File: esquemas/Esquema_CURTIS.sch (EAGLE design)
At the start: 18 parts

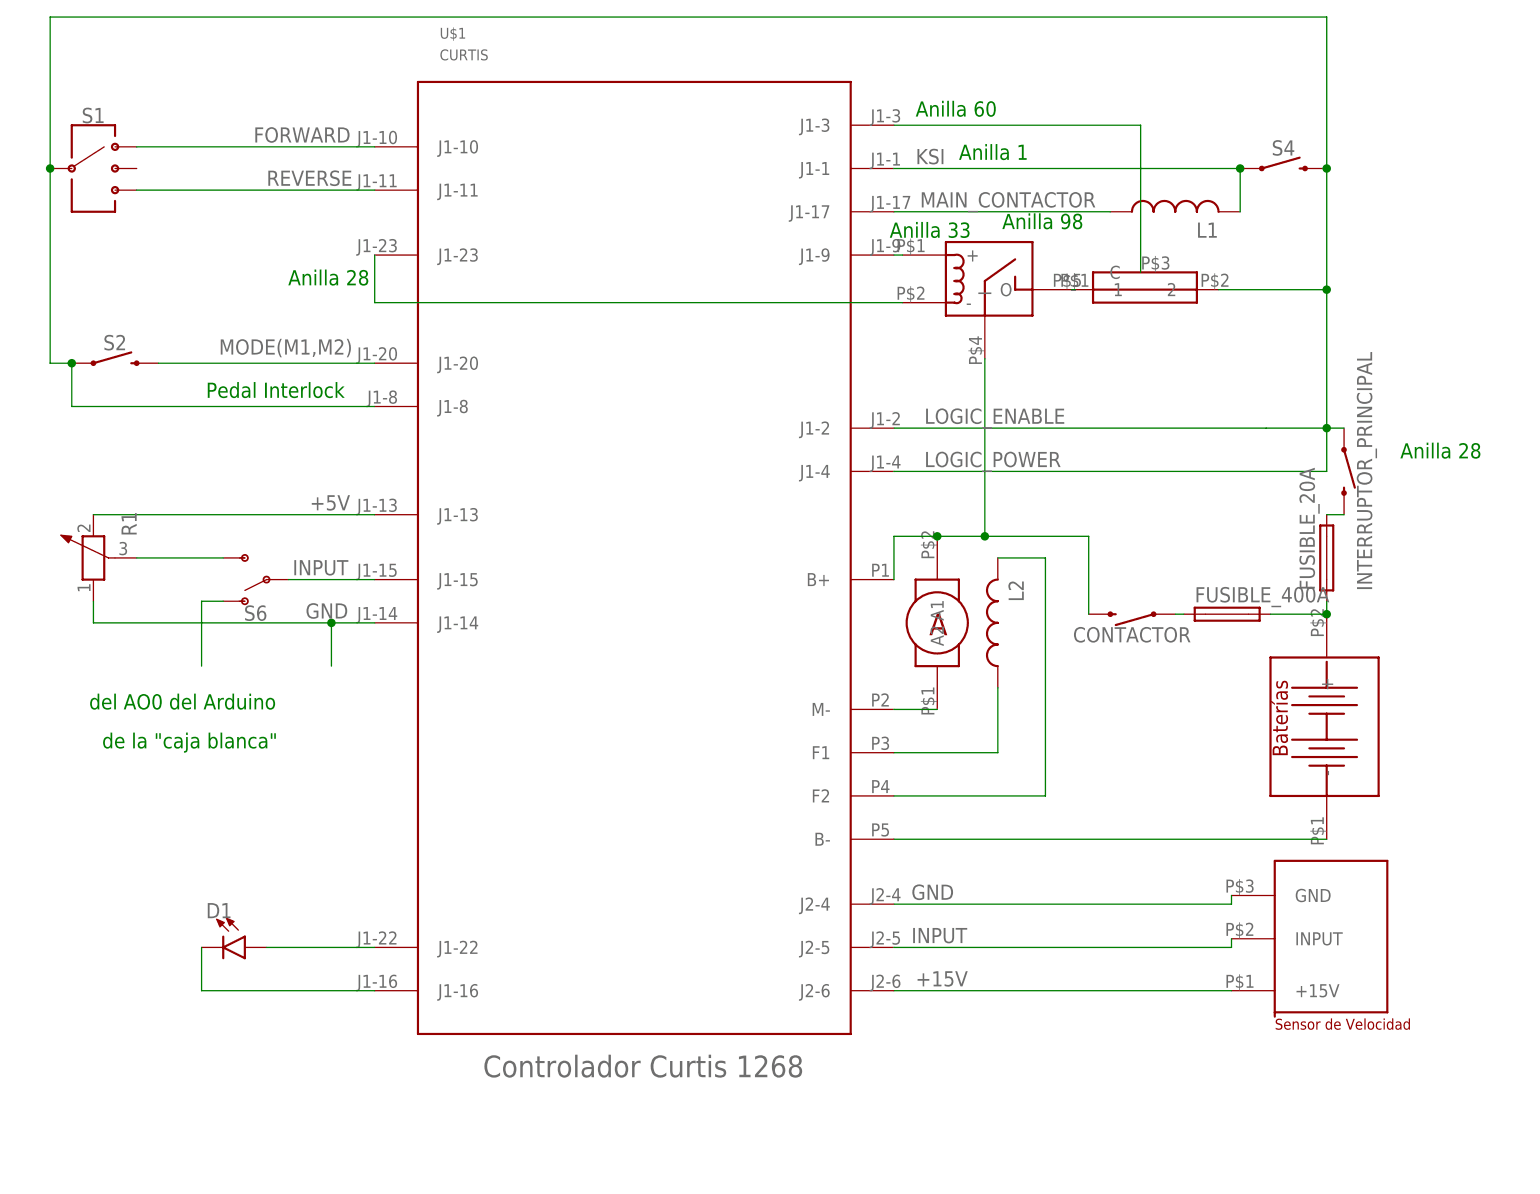
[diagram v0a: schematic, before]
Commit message: Modificación
Modificación del texto en PowerBox1, adición del programador en Curtis y
redistribución de algunos elementos
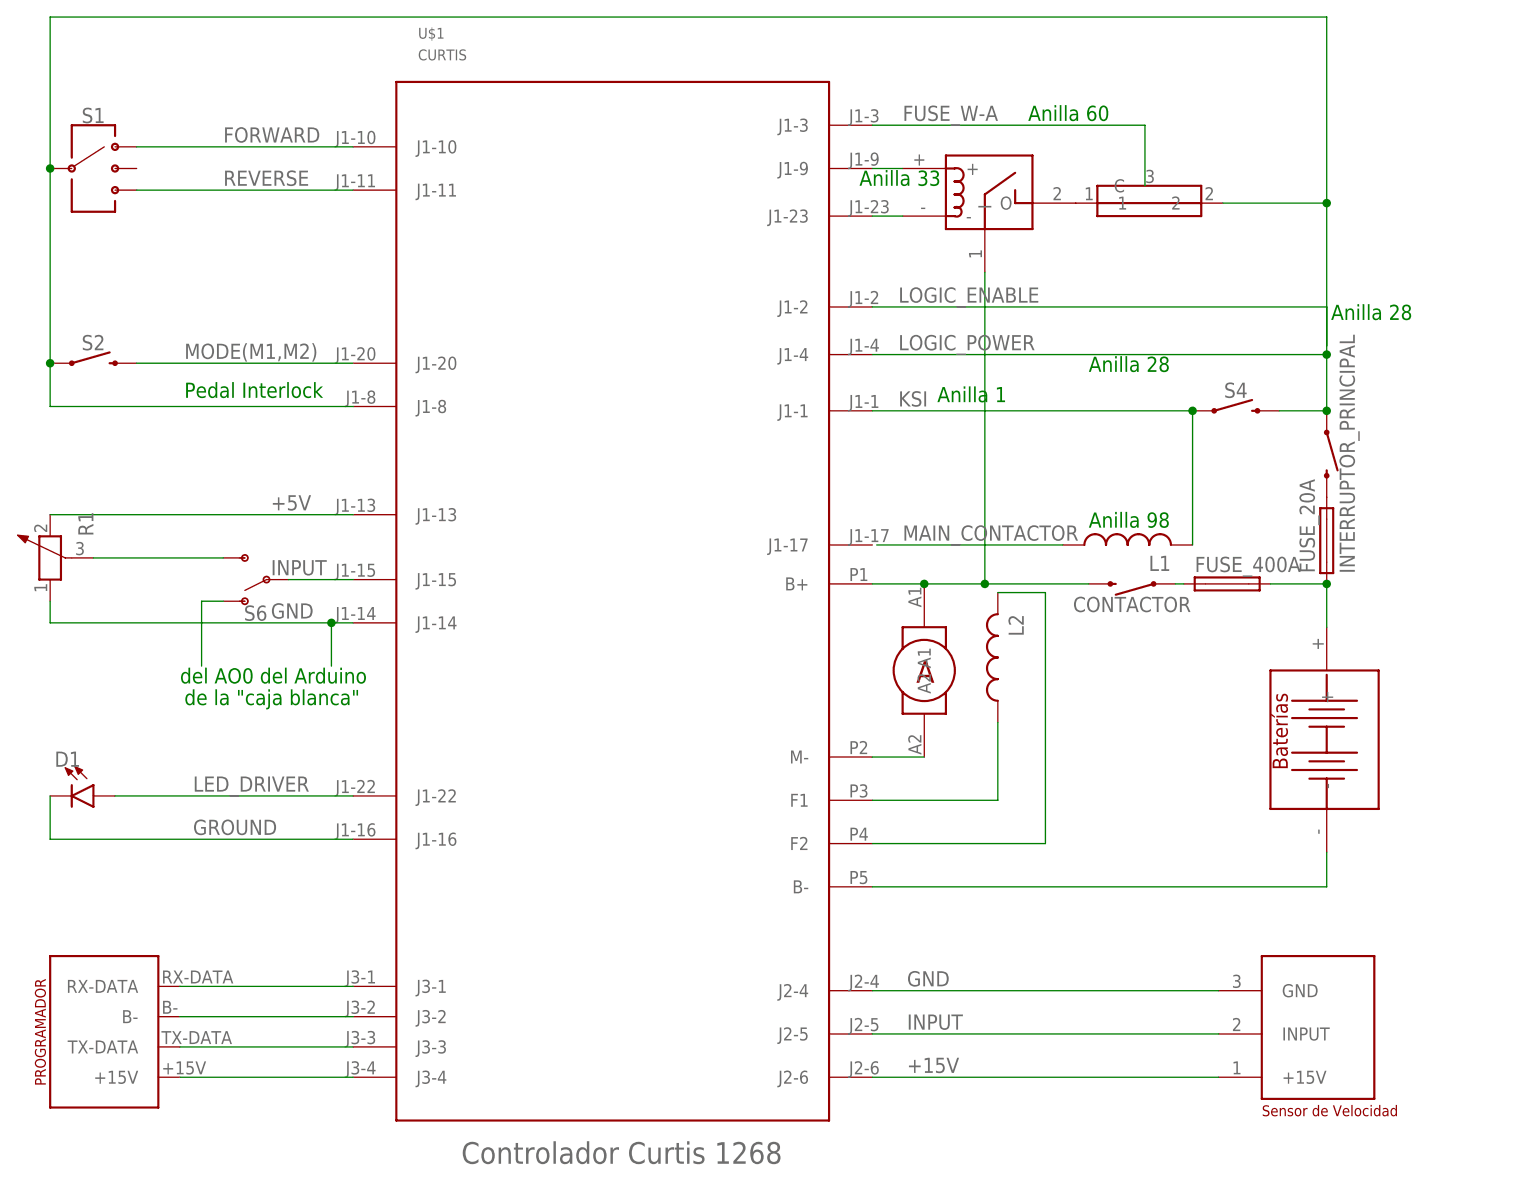
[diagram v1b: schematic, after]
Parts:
- removed FUSIBLE_20A, FUSIBLE_400A: (no value), fuse:GSH15
- added FUSE_20A, FUSE_400A: (no value), fuse:GSH15
- added U$3: PROGRAMADOR, ecar:PROGRAMADOR
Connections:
- net N$10 renamed GROUND
- net N$14 renamed FUSE_W-A
- net N$9 renamed LED_DRIVER
- removed net N$2 (its old number): U$1.M-, U$2.A2
- new net LOGIC_ENABLE: U$1.J1-2
- new net N$10: U$1.J3-2, U$3.B-
- new net N$12: U$1.J3-3, U$3.TX-DATA
- new net N$15: U$1.J3-4, U$3.+15V
- new net N$17: U$2.A2
- new net N$9: U$1.J3-1, U$3.RX-DATA
- net +15V: no longer U$1.J2-6
- net GND: no longer U$1.J2-4
- net INPUT: no longer U$1.J2-5
- net LOGIC_POWER: now also U$1.J1-4
- net MAIN_CONTACTOR: no longer U$1.J1-17
- net N$16: now also FUSE_20A.1, FUSE_400A.2; no longer FUSIBLE_20A.1, FUSIBLE_400A.2
- net N$3: now also FUSE_400A.1; no longer FUSIBLE_400A.1
- net N$4: no longer U$1.F1
- net N$5: now also FUSE_20A.2; no longer FUSIBLE_20A.2
- net N$8: no longer U$1.F2
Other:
- moved on the sheet: CONTACTOR, D1, INTERRUPTOR_PRINCIPAL, L1, L2, R1, S2, S4

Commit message: Conexión J1-1 a 48V
Modificación del interruptor denominado "Llave" de J1-1. Se suprime por
un cable a 48V
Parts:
- removed S4: (no value), SparkFun-Switches:MOMENTARY-SWITCH-SPST-PTH-6.0MM
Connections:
- removed net LOGIC_POWER: INTERRUPTOR_PRINCIPAL.1, S1.3, S2.1, S4.2, U$1.J1-4, U$1.J1-8, U$7.2
- net KSI: now also INTERRUPTOR_PRINCIPAL.1, S1.3, S2.1, U$1.J1-4, U$1.J1-8, U$7.2; no longer S4.1
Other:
- note added: "Anilla 4"
- note added: "Anilla 6"
- note added: "Anilla 67"
- note added: "Anilla 7"
- note added: "Anilla 90"
- note added: "Anilla 91"
- note added: "LOGIC_POWER"
- note added: "N"
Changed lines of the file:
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@@
 <setting verticaltext="up"/>
 </settings>
-<grid distance="0.02" unitdist="inch" unit="inch" style="lines" multiple="1" display="yes" altdistance="0.002" altunitdist="inch" altunit="inch"/>
+<grid distance="0.01" unitdist="inch" unit="inch" style="lines" multiple="1" display="yes" altdistance="0.001" altunitdist="inch" altunit="inch"/>
 <layers>
 <layer number="1" name="Top" color="4" fill="1" visible="no" active="no"/>
@@
 <part name="S1" library="SparkFun-Switches" deviceset="SWITCH-SP3T" device="-SMD"/>
 <part name="S2" library="SparkFun-Switches" deviceset="MOMENTARY-SWITCH-SPST" device="-PTH-6.0MM" value=" "/>
-<part name="S4" library="SparkFun-Switches" deviceset="MOMENTARY-SWITCH-SPST" device="-PTH-6.0MM" value=" "/>
 <part name="FUSE_20A" library="fuse" deviceset="GSH15" device=""/>
 <part name="R1" library="rcl" deviceset="POTENTIOMETER_" device="PT-10S"/>
@@
 <sheet>
 <plain>
-<text x="109.728" y="91.948" size="1.778" layer="91">Anilla 60</text>
+<text x="94.742" y="89.408" size="1.778" layer="91">Anilla 60</text>
 <text x="89.916" y="84.328" size="1.778" layer="91">Anilla 33</text>
 <text x="145.288" y="68.58" size="1.778" layer="91">Anilla 28</text>
 <text x="10.16" y="25.908" size="1.778" layer="91">del AO0 del Arduino</text>
 <text x="10.668" y="23.368" size="1.778" layer="91">de la "caja blanca"</text>
-<text x="116.84" y="62.484" size="1.778" layer="91">Anilla 28</text>
-<text x="99.06" y="58.928" size="1.778" layer="91">Anilla 1</text>
-<text x="116.84" y="44.196" size="1.778" layer="91">Anilla 98</text>
+<text x="112.014" y="67.818" size="1.778" layer="91">Anilla 28</text>
+<text x="112.268" y="55.372" size="1.778" layer="91">Anilla 1</text>
+<text x="108.204" y="39.878" size="1.778" layer="91">Anilla 98</text>
 <text x="10.668" y="59.436" size="1.778" layer="91">Pedal Interlock</text>
+<text x="88.9" y="77.724" size="1.778" layer="91">Anilla 28</text>
+<text x="22.86" y="43.18" size="1.778" layer="91">Anilla 6</text>
+<text x="25.654" y="30.48" size="1.778" layer="91">Anilla 7</text>
+<text x="24.13" y="36.068" size="1.778" layer="91">Anilla 4</text>
+<text x="5.588" y="86.106" size="1.778" layer="91">N</text>
+<text x="23.368" y="86.614" size="1.778" layer="91">Anilla 90</text>
+<text x="23.622" y="81.026" size="1.778" layer="91">Anilla 91</text>
+<text x="112.014" y="62.23" size="1.778" layer="91">Anilla 67</text>
+<text x="94.742" y="65.024" size="1.778" layer="91">LOGIC_POWER</text>
 </plain>
 <instances>
 <instance part="S1" gate="G$1" x="0" y="86.36"/>
 <instance part="S2" gate="G$1" x="0" y="63.5"/>
-<instance part="S4" gate="G$1" x="134.112" y="57.912"/>
 <instance part="FUSE_20A" gate="1" x="144.78" y="42.672" rot="R90"/>
 <instance part="R1" gate="1" x="-5.08" y="40.64" rot="R90"/>
@@
 </segment>
 </net>
-<net name="KSI" class="0">
-<segment>
-<pinref part="S4" gate="G$1" pin="1"/>
-<wire x1="129.032" y1="57.912" x2="91.44" y2="57.912" width="0.1524" layer="91"/>
-<pinref part="L1" gate="G$1" pin="2"/>
-<wire x1="129.032" y1="42.164" x2="129.032" y2="57.912" width="0.1524" layer="91"/>
-<junction x="129.032" y="57.912"/>
-<label x="94.488" y="58.42" size="1.778" layer="95"/>
-<pinref part="U$1" gate="G$1" pin="J1-1"/>
-</segment>
-</net>
 <net name="MAIN_CONTACTOR" class="0">
 <segment>
@@
 </segment>
 </net>
-<net name="LOGIC_POWER" class="0">
+<net name="LED_DRIVER" class="0">
+<segment>
+<wire x1="30.48" y1="12.7" x2="2.54" y2="12.7" width="0.1524" layer="91"/>
+<pinref part="D1" gate="G$1" pin="A"/>
+<label x="11.684" y="13.208" size="1.778" layer="95"/>
+<pinref part="U$1" gate="G$1" pin="J1-22"/>
+</segment>
+</net>
+<net name="GROUND" class="0">
+<segment>
+<pinref part="D1" gate="G$1" pin="C"/>
+<wire x1="-5.08" y1="12.7" x2="-5.08" y2="7.62" width="0.1524" layer="91"/>
+<wire x1="-5.08" y1="7.62" x2="30.48" y2="7.62" width="0.1524" layer="91"/>
+<label x="11.684" y="8.128" size="1.778" layer="95"/>
+<pinref part="U$1" gate="G$1" pin="J1-16"/>
+</segment>
+</net>
+<net name="N$9" class="0">
+<segment>
+<pinref part="U$3" gate="G$1" pin="RX-DATA"/>
+<wire x1="10.16" y1="-9.652" x2="30.48" y2="-9.652" width="0.1524" layer="91"/>
+<pinref part="U$1" gate="G$1" pin="J3-1"/>
+</segment>
+</net>
+<net name="N$10" class="0">
+<segment>
+<pinref part="U$3" gate="G$1" pin="B-"/>
+<wire x1="30.48" y1="-13.208" x2="10.16" y2="-13.208" width="0.1524" layer="91"/>
+<pinref part="U$1" gate="G$1" pin="J3-2"/>
+</segment>
+</net>
+<net name="N$12" class="0">
+<segment>
+<pinref part="U$3" gate="G$1" pin="TX-DATA"/>
+<wire x1="30.48" y1="-16.764" x2="10.16" y2="-16.764" width="0.1524" layer="91"/>
+<pinref part="U$1" gate="G$1" pin="J3-3"/>
+</segment>
+</net>
+<net name="N$15" class="0">
+<segment>
+<pinref part="U$3" gate="G$1" pin="+15V"/>
+<wire x1="30.48" y1="-20.32" x2="10.16" y2="-20.32" width="0.1524" layer="91"/>
+<pinref part="U$1" gate="G$1" pin="J3-4"/>
+</segment>
+</net>
+<net name="N$17" class="0">
+<segment>
+<pinref part="U$2" gate="G$1" pin="A2"/>
+<wire x1="97.536" y1="17.272" x2="91.44" y2="17.272" width="0.1524" layer="91"/>
+</segment>
+</net>
+<net name="N$2" class="0">
+<segment>
+<pinref part="U$7" gate="G$1" pin="1"/>
+<pinref part="U$6" gate="G$1" pin="O"/>
+</segment>
+</net>
+<net name="N$13" class="0">
+<segment>
+<pinref part="U$6" gate="G$1" pin="-"/>
+<pinref part="U$1" gate="G$1" pin="J1-23"/>
+<wire x1="94.996" y1="80.772" x2="91.44" y2="80.772" width="0.1524" layer="91"/>
+</segment>
+</net>
+<net name="KSI" class="0">
 <segment>
 <pinref part="S2" gate="G$1" pin="1"/>
@@
 <wire x1="144.78" y1="57.912" x2="144.78" y2="64.516" width="0.1524" layer="91"/>
 <wire x1="91.44" y1="64.516" x2="144.78" y2="64.516" width="0.1524" layer="91"/>
-<label x="94.488" y="65.024" size="1.778" layer="95"/>
 <wire x1="144.78" y1="104.14" x2="144.78" y2="82.296" width="0.1524" layer="91"/>
 <junction x="144.78" y="82.296"/>
-<pinref part="S4" gate="G$1" pin="2"/>
-<wire x1="139.192" y1="57.912" x2="144.78" y2="57.912" width="0.1524" layer="91"/>
 <pinref part="INTERRUPTOR_PRINCIPAL" gate="G$1" pin="1"/>
 <junction x="144.78" y="57.912"/>
 <pinref part="U$1" gate="G$1" pin="J1-8"/>
 <pinref part="U$1" gate="G$1" pin="J1-4"/>
-</segment>
-</net>
-<net name="LED_DRIVER" class="0">
-<segment>
-<wire x1="30.48" y1="12.7" x2="2.54" y2="12.7" width="0.1524" layer="91"/>
-<pinref part="D1" gate="G$1" pin="A"/>
-<label x="11.684" y="13.208" size="1.778" layer="95"/>
-<pinref part="U$1" gate="G$1" pin="J1-22"/>
-</segment>
-</net>
-<net name="GROUND" class="0">
-<segment>
-<pinref part="D1" gate="G$1" pin="C"/>
-<wire x1="-5.08" y1="12.7" x2="-5.08" y2="7.62" width="0.1524" layer="91"/>
-<wire x1="-5.08" y1="7.62" x2="30.48" y2="7.62" width="0.1524" layer="91"/>
-<label x="11.684" y="8.128" size="1.778" layer="95"/>
-<pinref part="U$1" gate="G$1" pin="J1-16"/>
-</segment>
-</net>
-<net name="N$9" class="0">
-<segment>
-<pinref part="U$3" gate="G$1" pin="RX-DATA"/>
-<wire x1="10.16" y1="-9.652" x2="30.48" y2="-9.652" width="0.1524" layer="91"/>
-<pinref part="U$1" gate="G$1" pin="J3-1"/>
-</segment>
-</net>
-<net name="N$10" class="0">
-<segment>
-<pinref part="U$3" gate="G$1" pin="B-"/>
-<wire x1="30.48" y1="-13.208" x2="10.16" y2="-13.208" width="0.1524" layer="91"/>
-<pinref part="U$1" gate="G$1" pin="J3-2"/>
-</segment>
-</net>
-<net name="N$12" class="0">
-<segment>
-<pinref part="U$3" gate="G$1" pin="TX-DATA"/>
-<wire x1="30.48" y1="-16.764" x2="10.16" y2="-16.764" width="0.1524" layer="91"/>
-<pinref part="U$1" gate="G$1" pin="J3-3"/>
-</segment>
-</net>
-<net name="N$15" class="0">
-<segment>
-<pinref part="U$3" gate="G$1" pin="+15V"/>
-<wire x1="30.48" y1="-20.32" x2="10.16" y2="-20.32" width="0.1524" layer="91"/>
-<pinref part="U$1" gate="G$1" pin="J3-4"/>
-</segment>
-</net>
-<net name="N$17" class="0">
-<segment>
-<pinref part="U$2" gate="G$1" pin="A2"/>
-<wire x1="97.536" y1="17.272" x2="91.44" y2="17.272" width="0.1524" layer="91"/>
-</segment>
-</net>
-<net name="N$2" class="0">
-<segment>
-<pinref part="U$7" gate="G$1" pin="1"/>
-<pinref part="U$6" gate="G$1" pin="O"/>
-</segment>
-</net>
-<net name="N$13" class="0">
-<segment>
-<pinref part="U$6" gate="G$1" pin="-"/>
-<pinref part="U$1" gate="G$1" pin="J1-23"/>
-<wire x1="94.996" y1="80.772" x2="91.44" y2="80.772" width="0.1524" layer="91"/>
-</segment>
-</net>
+<wire x1="129.032" y1="57.912" x2="91.44" y2="57.912" width="0.1524" layer="91"/>
+<pinref part="L1" gate="G$1" pin="2"/>
+<wire x1="129.032" y1="42.164" x2="129.032" y2="57.912" width="0.1524" layer="91"/>
+<label x="94.488" y="58.42" size="1.778" layer="95"/>
+<pinref part="U$1" gate="G$1" pin="J1-1"/>
+<wire x1="144.78" y1="57.912" x2="129.032" y2="57.912" width="0.1524" layer="91"/>
+<junction x="129.032" y="57.912"/>
+</segment>
+</net>
